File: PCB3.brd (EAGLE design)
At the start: 100 x 80 mm, 48 parts

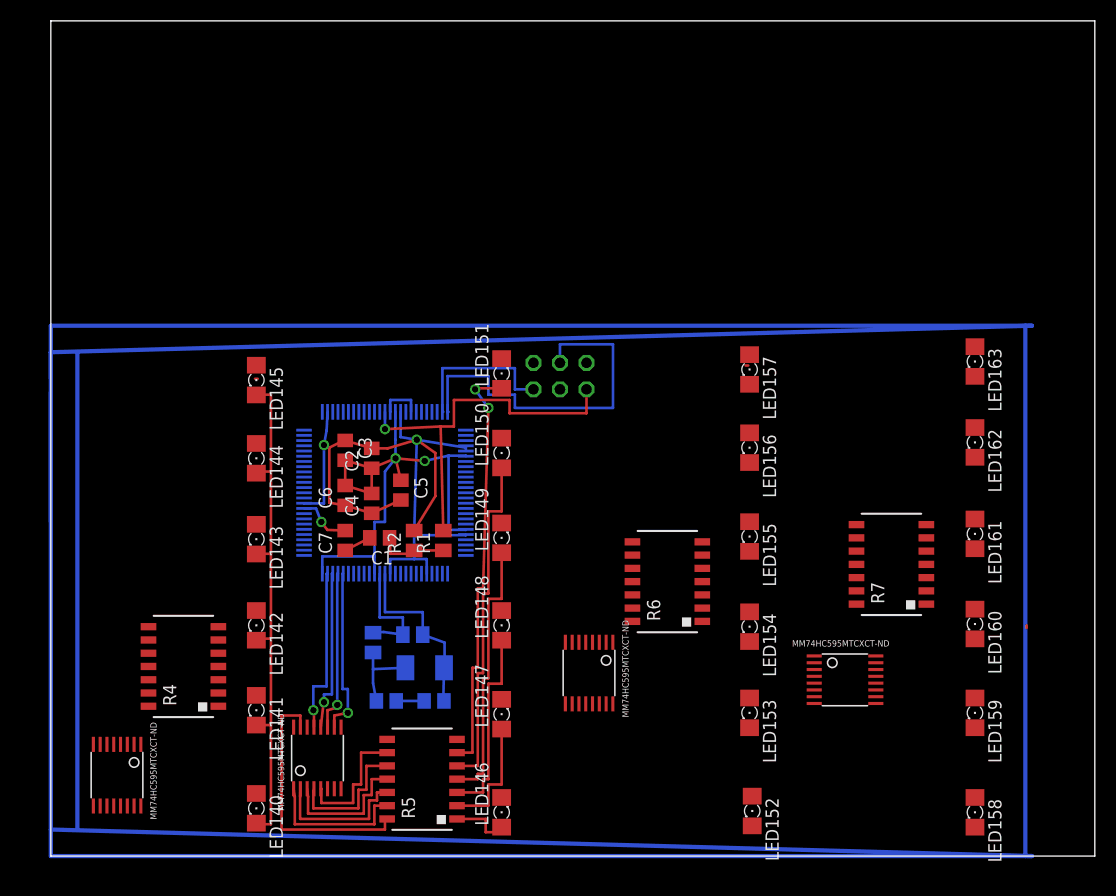
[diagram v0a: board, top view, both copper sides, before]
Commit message: Finished the remaining component traces for PCB3 layout, but not the traces to other boards
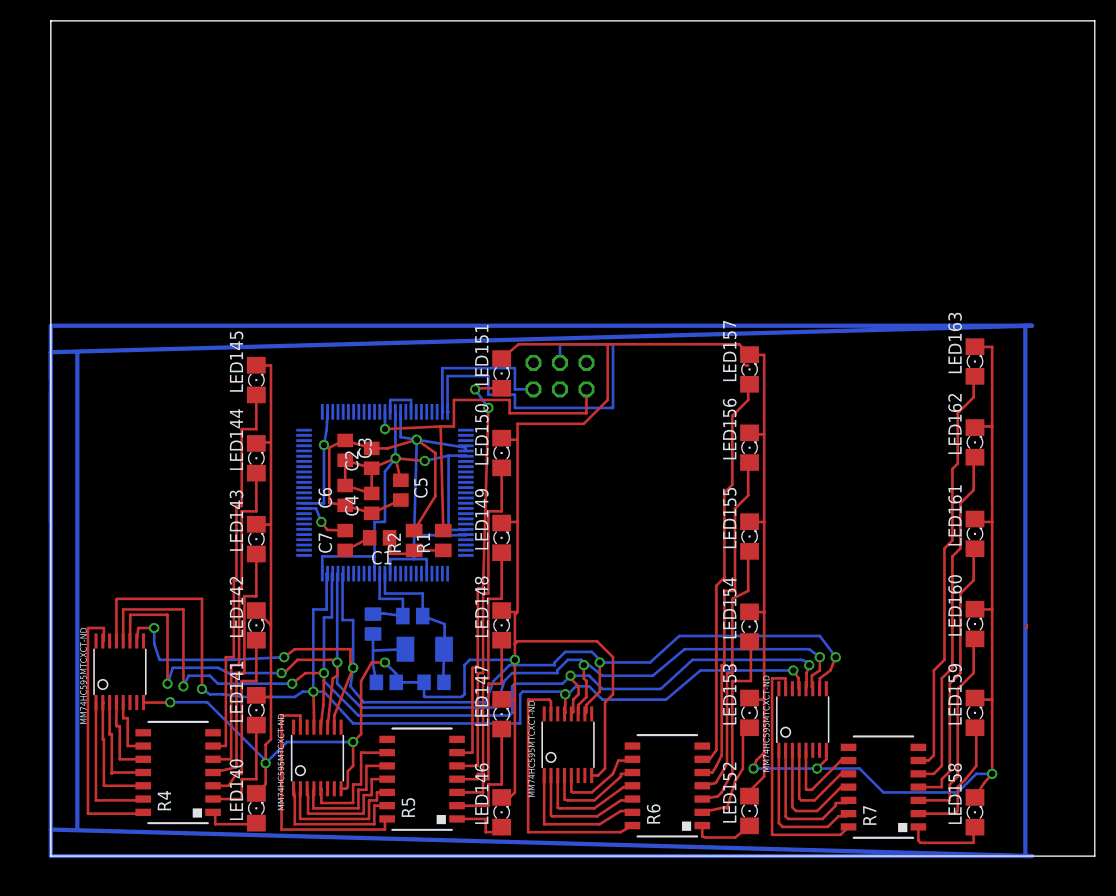
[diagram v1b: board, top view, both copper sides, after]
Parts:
- moved R7 21.3 mm to (79.8, 6.60)
- moved R6 19.6 mm to (59.1, 6.73)
- moved R4 10.2 mm to (12.2, 8.00)
- moved U$27 9.91 mm to (6.60, 17.7), turned to 0 degrees
- moved U$29 7.15 mm to (49.5, 10.7), turned to 0 degrees
- moved U$26 5.57 mm to (72.0, 13.1), turned to 0 degrees
- moved R3 1.78 mm to (30.9, 22.2)
- moved Y1 1.78 mm to (35.8, 19.8)
- moved C8 1.78 mm to (36.7, 16.6)
- moved C9 1.78 mm to (32.1, 16.6)
- moved R8 1.78 mm to (34.7, 23.0)
- moved LED152 0.25 mm to (66.9, 4.32), turned to 90 degrees
- turned LED140 to 90 degrees
- turned LED141 to 90 degrees
- turned LED142 to 90 degrees
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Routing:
- net GND: track 52.7 -> 341.5 mm, vias 0 -> 8
- net SCK: track 15.5 -> 108.3 mm, vias 1 -> 5
- net RCK: track 15.6 -> 106.6 mm, vias 1 -> 5
- net SCLR: track 16.3 -> 105.8 mm, vias 1 -> 5
- net G: track 16.1 -> 103.9 mm, vias 1 -> 4
- net N$136: track 0.00 -> 39.6 mm
- net N$101: track 0.00 -> 38.2 mm
- net N$47: track 0.00 -> 37.8 mm
- net N$135: track 0.00 -> 33.4 mm
- net N$100: track 0.00 -> 32.7 mm
- net N$46: track 0.00 -> 31.6 mm
- net N$134: track 0.00 -> 26.4 mm
- net N$96: track 0.00 -> 26.3 mm
- net N$31: track 0.00 -> 26.1 mm
- net N$99: track 0.00 -> 25.3 mm
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
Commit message: Added oscillator schematic to Stamp Board and started layout corrections.
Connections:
- net N$30 renamed FRET16
- net N$43 renamed FRET17
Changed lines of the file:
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@@
 <?xml version="1.0" encoding="utf-8"?>
 <!DOCTYPE eagle SYSTEM "eagle.dtd">
-<eagle version="8.0.1">
+<eagle version="8.0.0">
 <drawing>
 <settings>
@@
 <wire x1="30.861" y1="18.349" x2="31.181" y2="16.637" width="0.254" layer="16"/>
 </signal>
-<signal name="N$30">
+<signal name="FRET16">
 <contactref element="R8" pad="1"/>
 <contactref element="R3" pad="2"/>
@@
 <contactref element="U$2" pad="26"/>
 </signal>
-<signal name="N$43">
+<signal name="FRET17">
 <contactref element="U$2" pad="27"/>
 </signal>

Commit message: Changed most pins on micro and condensed all of the connections on PCB3. Began making traces for other PCBs from PCB3 and created GRN plane for PCB3.
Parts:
- moved R3 2.92 mm to (30.9, 19.3)
- moved Y1 2.82 mm to (36.2, 17.0)
- moved C9 2.81 mm to (31.9, 13.8)
- moved C8 2.81 mm to (37.0, 13.8)
- moved R8 2.54 mm to (34.7, 20.4)
- moved U$28 0.57 mm to (25.0, 9.14)
- moved R1 0.57 mm to (37.3, 30.7)
- moved R2 0.51 mm to (34.8, 30.7)
- moved C1 0.25 mm to (31.5, 30.2)
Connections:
- removed net N$103: U$29.14
- removed net N$138: U$26.14
- removed net N$3: U$2.17
- removed net N$4: U$2.22
- removed net N$42: U$2.26
- removed net N$44: U$2.28
- removed net N$45: U$2.29
- removed net N$48: U$27.14
- removed net N$5: U$2.23
- removed net N$50: U$2.36
- removed net N$51: U$2.37
- removed net N$52: U$2.38
- removed net N$66: U$2.54
- removed net N$67: U$2.56
- removed net N$68: U$2.57
- removed net N$85: U$28.14
- removed net PE: C1.2, C7.1
- new net EAN: U$2.79
- new net OSC2: R3.2, R8.1, U$2.64
- new net P1_2: U$2.76
- new net P1_3: U$2.77
- new net P2_0: U$2.81
- new net P2_4: U$2.80
- new net P3_6: U$2.7
- net FRET1: now also U$2.93; no longer U$2.41
- net FRET10: now also U$2.26; no longer U$2.52
- net FRET11: now also U$2.27; no longer U$2.53
- net FRET12: now also U$2.28; no longer U$2.58
- net FRET13: now also U$2.29; no longer U$2.59
- net FRET14: now also U$2.32; no longer U$2.60
- net FRET15: now also U$2.33; no longer U$2.61
- net FRET16: now also U$2.34; no longer R3.2, R8.1, U$2.64
- net FRET17: now also U$2.35; no longer U$2.27
- net FRET18: now also U$2.36; no longer U$2.66
- net FRET19: now also U$2.37; no longer U$2.67
- net FRET2: now also U$2.92; no longer U$2.42
- net FRET20: now also U$2.38; no longer U$2.68
- net FRET21: now also U$2.39; no longer U$2.69
- net FRET22: now also U$2.40; no longer U$2.70
- net FRET3: now also U$2.91; no longer U$2.43
- net FRET4: now also U$2.90; no longer U$2.44
- net FRET5: now also U$2.19; no longer U$2.47
- net FRET6: now also U$2.20; no longer U$2.48
- net FRET7: now also U$2.21; no longer U$2.49
- net FRET8: now also U$2.22; no longer U$2.50
- net FRET9: now also U$2.23; no longer U$2.51
- net G: now also U$2.69; no longer U$2.74
- net GND: now also C1.2, C7.1
- net LED_SER10: now also U$2.70, U$28.14; no longer U$2.91
- net LED_SER11: now also U$2.61, U$29.14; no longer U$2.90
- net LED_SER12: now also U$2.51; no longer U$2.89
- net LED_SER13: now also U$2.58; no longer U$2.88
- net LED_SER14: now also U$2.59; no longer U$2.87
- net LED_SER15: now also U$2.53; no longer U$2.84
- net LED_SER16: now also U$2.52; no longer U$2.83
- net LED_SER17: now also U$2.41; no longer U$2.82
- net LED_SER18: now also U$2.42; no longer U$2.81
- net LED_SER19: now also U$2.43; no longer U$2.80
- net LED_SER20: now also U$2.44; no longer U$2.79
- net LED_SER21: now also U$2.47; no longer U$2.78
- net LED_SER22: now also U$2.48; no longer U$2.77
- net LED_SER23: now also U$2.49; no longer U$2.76
- net LED_SER5: now also U$2.74; no longer U$2.96
- net LED_SER6: now also U$2.73; no longer U$2.95
- net LED_SER7: now also U$2.72; no longer U$2.94
- net LED_SER8: now also U$2.60, U$26.14; no longer U$2.93
- net LED_SER9: now also U$2.71, U$27.14; no longer U$2.92
- net P0_0: now also U$2.82; no longer U$2.14, U$2.18
- net P0_5: now also U$2.83; no longer U$2.12
- net P1_7: now also U$2.84; no longer U$2.19
- net P3_7: now also U$2.6; no longer U$2.7
- net RCK: now also U$2.68; no longer U$2.73
- net RST_N: now also U$2.78; no longer U$2.6
- net RXD: now also U$2.14; no longer U$2.21
- net SCK: now also U$2.67; no longer U$2.72
- net SCLR: now also U$2.66; no longer U$2.71
- net STRING1: now also U$2.96; no longer U$2.32
- net STRING2: now also U$2.95; no longer U$2.33
- net STRING3: now also U$2.94; no longer U$2.34
- net STRING4: now also U$2.89; no longer U$2.35
- net STRING5: now also U$2.88; no longer U$2.39
- net STRING6: now also U$2.87; no longer U$2.40
- net TXD: now also U$2.12; no longer U$2.20
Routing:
- net GND: track 341.5 -> 57.0 mm, vias 8 -> 24
- net N$6: track 283.2 -> 94.0 mm
- net N$11: track 193.1 -> 94.0 mm
- net LED_SER8: track 0.00 -> 73.9 mm, vias 0 -> 1
- net LED_SER9: track 0.00 -> 53.9 mm, vias 0 -> 1
- net N$8: track 45.7 -> 0.00 mm
- net G: track 103.9 -> 147.6 mm
- net RCK: track 106.6 -> 150.1 mm
- net SCLR: track 105.8 -> 147.1 mm
- net SCK: track 108.3 -> 149.5 mm
- net LED_SER11: track 0.00 -> 26.2 mm, vias 0 -> 1
- net P1_2: track 0.00 -> 25.7 mm
- net EAN: track 0.00 -> 25.5 mm
- net P2_4: track 0.00 -> 25.4 mm
- net RST_N: track 0.00 -> 25.4 mm
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- added copper zone on layer 16, net GND

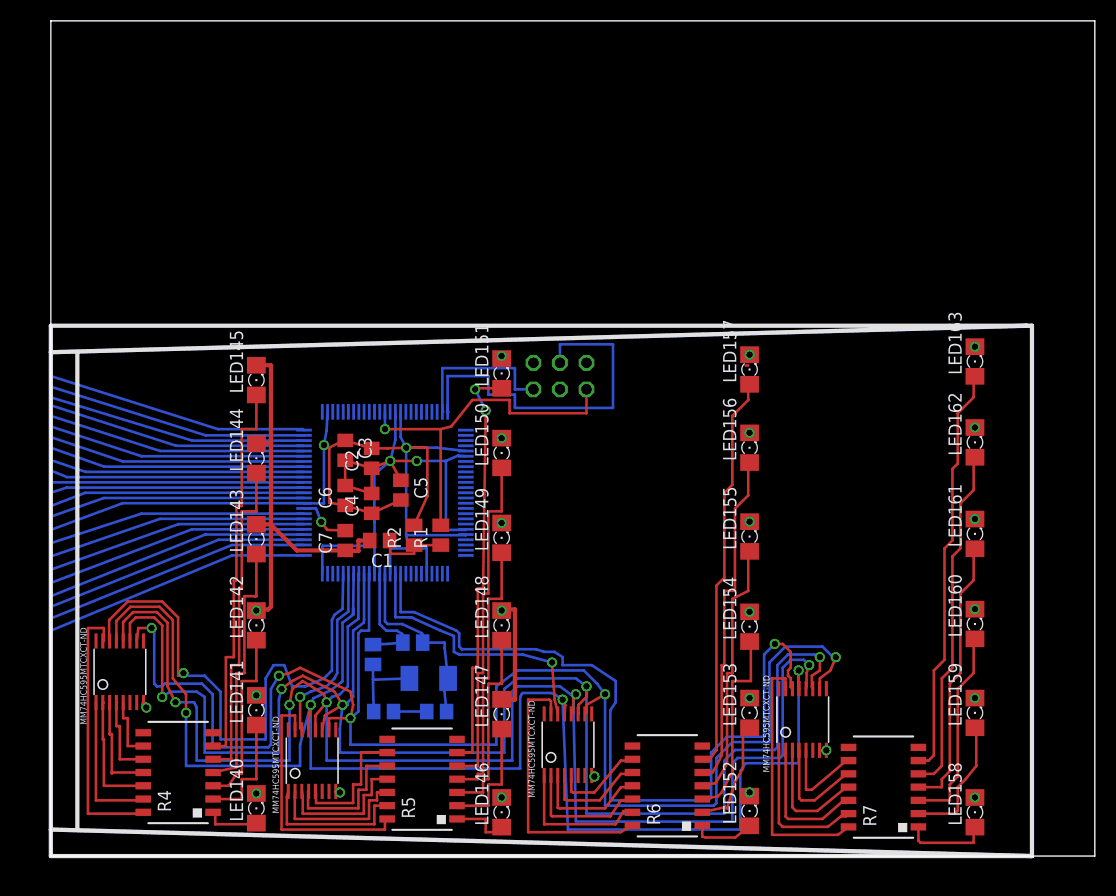
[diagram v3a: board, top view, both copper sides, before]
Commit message: Added pads for frets, redid traces from micro to other PCBs
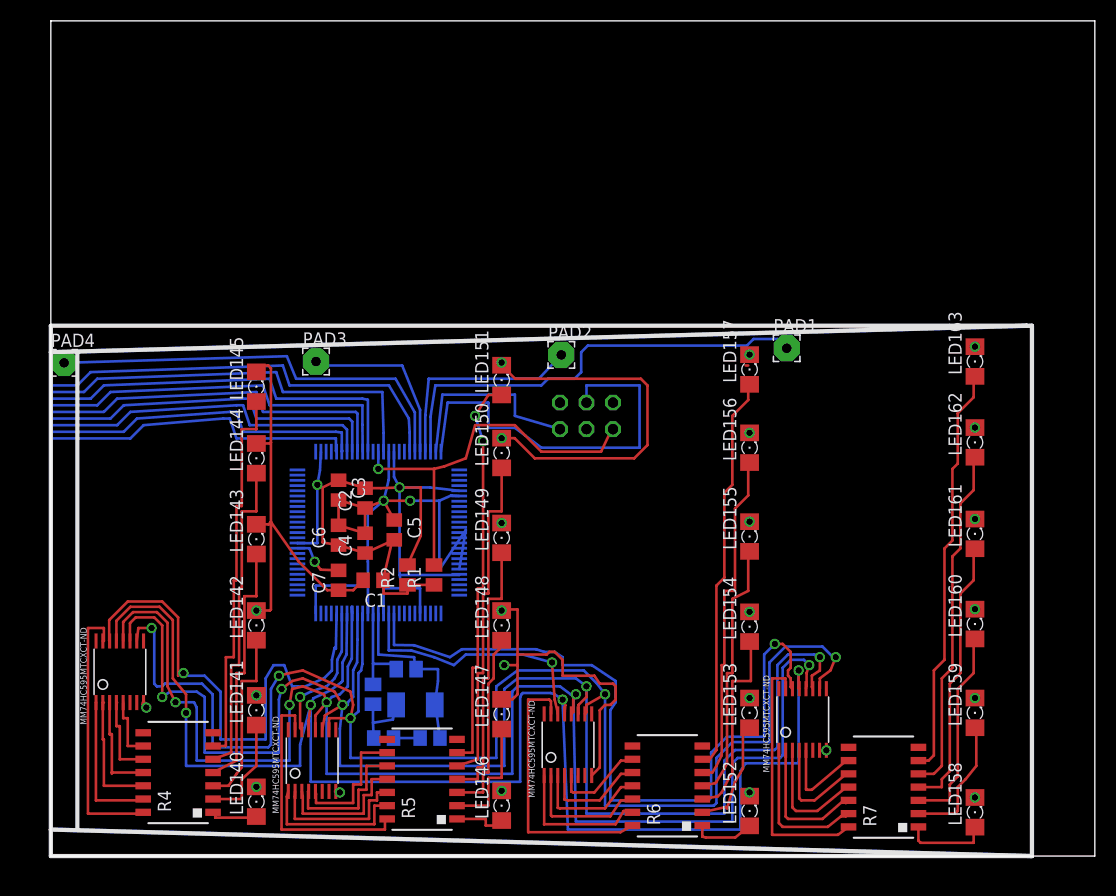
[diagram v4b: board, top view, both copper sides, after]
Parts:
- added PAD1, PAD2, PAD3, PAD4: WIREPAD2,54/0,9, wirepad:2,54/0,9
- moved ICSP 4.58 mm to (51.3, 42.2)
- moved C2 3.86 mm to (30.1, 34.3)
- moved R2 3.86 mm to (34.2, 26.9)
- moved C3 3.86 mm to (27.6, 35.1)
- moved R1 3.86 mm to (36.7, 26.9)
- moved U$2 3.86 mm to (31.4, 31.0)
- moved C1 3.86 mm to (30.9, 26.4)
- moved C5 3.86 mm to (32.9, 31.2)
- moved C7 3.86 mm to (27.6, 26.4)
- moved C4 3.86 mm to (30.1, 30.0)
- moved C6 3.86 mm to (27.6, 30.7)
- moved R3 3.81 mm to (30.9, 15.5)
- moved Y1 2.84 mm to (34.9, 14.5)
- moved C8 2.62 mm to (36.3, 11.3)
- moved R8 2.62 mm to (34.0, 17.9)
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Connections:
- net FRET6: now also PAD4.1
- net FRET7: now also PAD3.1
- net FRET8: now also PAD2.1
- net FRET9: now also PAD1.1
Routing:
- net GND: track 57.0 -> 116.0 mm
- net FRET9: track 0.00 -> 43.4 mm
- net FRET5: track 0.00 -> 41.2 mm
- net FRET6: track 0.00 -> 40.7 mm
- net RXD: track 0.00 -> 39.4 mm
- net P3_1: track 0.00 -> 37.3 mm
- net P3_2: track 0.00 -> 36.2 mm
- net P3_3: track 0.00 -> 35.0 mm
- net P3_4: track 0.00 -> 33.8 mm
- net P3_6: track 0.00 -> 32.6 mm
- net P3_7: track 0.00 -> 31.7 mm
- net WAKEUP: track 0.00 -> 30.5 mm
- net P1_2: track 25.7 -> 0.00 mm
- net EAN: track 25.5 -> 0.00 mm
- net P2_4: track 25.4 -> 0.00 mm
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
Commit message: Finished routing traces for both sides of micro
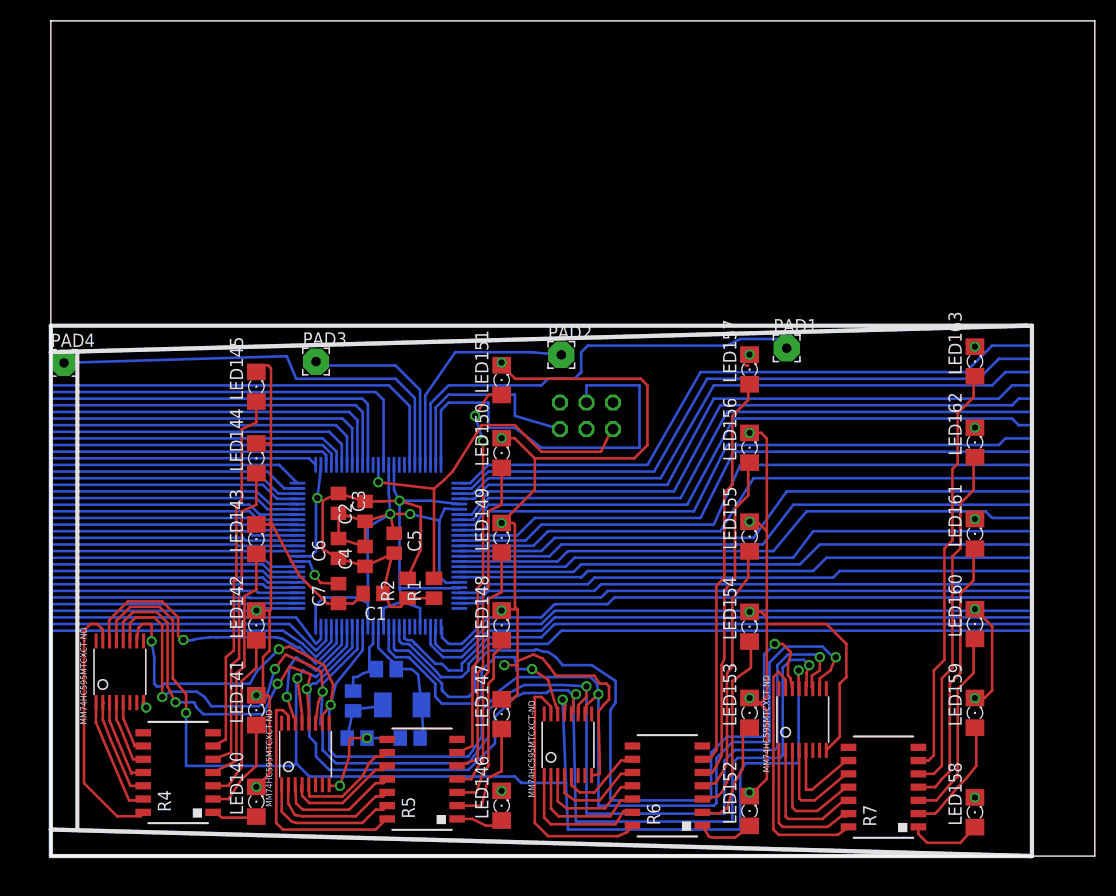
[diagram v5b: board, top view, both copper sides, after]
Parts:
- moved C9 2.54 mm to (29.3, 11.3)
- moved R3 2.01 mm to (29.0, 14.9)
- moved C8 1.91 mm to (34.4, 11.3)
- moved R8 1.91 mm to (32.1, 17.9)
- moved C3 1.27 mm to (27.6, 33.8)
- moved C6 1.27 mm to (27.6, 29.5)
- moved C1 1.27 mm to (30.9, 25.1)
- moved C4 1.27 mm to (30.1, 28.7)
- moved C5 1.27 mm to (32.9, 30.0)
- moved C7 1.27 mm to (27.6, 25.1)
- moved R1 1.27 mm to (36.7, 25.7)
- moved R2 1.27 mm to (34.2, 25.7)
- moved U$2 1.27 mm to (31.4, 29.7)
- moved C2 1.27 mm to (30.1, 33.0)
- moved Y1 1.27 mm to (33.7, 14.5)
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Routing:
- net GND: track 116.0 -> 231.2 mm
- net LED_SER14: track 0.00 -> 65.6 mm
- net LED_SER13: track 0.00 -> 64.9 mm
- net FRET10: track 0.00 -> 61.8 mm
- net FRET11: track 0.00 -> 61.5 mm
- net LED_SER15: track 0.00 -> 61.4 mm
- net FRET14: track 0.00 -> 61.2 mm
- net FRET12: track 0.00 -> 61.2 mm
- net FRET16: track 0.00 -> 61.1 mm
- net FRET15: track 0.00 -> 60.9 mm
- net FRET13: track 0.00 -> 60.9 mm
- net LED_SER16: track 0.00 -> 60.6 mm
- net FRET17: track 0.00 -> 60.5 mm
- net LED_SER12: track 0.00 -> 59.6 mm
- net FRET18: track 0.00 -> 59.5 mm
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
